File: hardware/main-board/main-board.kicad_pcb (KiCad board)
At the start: 2 copper layers, 48 x 48 mm, 44 parts, among them J1 USB-C Receptacle, J2 JST JWPF, J3 LCD_FFC_SOLDER, Q1 SS8050-G, Q2 SS8050-G, Q3 SS8050-G, SW1 FRONT_BUTTON, U1 SN65HVD230, U2 CPC1017N, U3 AP1509-33SG-13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

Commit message: layout almost done
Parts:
- moved D1 2.29 mm to (-14.1, 11.4)
- moved C3 1.91 mm to (12.8, 1.02)
- moved R11 0.51 mm to (-15.6, -2.41)
- moved R9 0.44 mm to (-15.7, 0.64)
- moved U4 0.38 mm to (-19.7, -0.60)
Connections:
- D1 pad 1: /USB_D+ -> /USB_D-
- D1 pad 3: /USB_D- -> /USB_D+
- R4 pad 2: (no net) -> /ESP32/CANBUS_TERM_EN
- U5 pad 24: (no net) -> /ESP32/CANBUS_TERM_EN
- U5 pad 39: (no net) -> GND
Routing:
- net +3V3: track 0.00 -> 62.4 mm, vias 0 -> 3
- net /USB_VBUS: track 0.00 -> 60.2 mm, vias 0 -> 4
- net /ESP32/EN: track 0.00 -> 55.0 mm, vias 0 -> 2
- net /ESP32/FRONT_BUTTON: track 0.00 -> 39.4 mm, vias 0 -> 1
- net /ESP32/PROG_TXD: track 0.00 -> 32.2 mm, vias 0 -> 2
- net /ESP32/PROG_RX: track 0.00 -> 32.2 mm, vias 0 -> 2
- net /USB_D+: track 0.00 -> 29.5 mm, vias 0 -> 2
- net /USB_D-: track 0.00 -> 27.0 mm, vias 0 -> 3
- net /ESP32/IO0: track 0.00 -> 24.3 mm, vias 0 -> 2
- net /LCD/BACKLIGHT: track 0.00 -> 22.6 mm, vias 0 -> 2
- net /ESP32/LCD_SDO: track 0.00 -> 22.5 mm, vias 0 -> 1
- net /ESP32/CANBUS_TX: track 0.00 -> 22.3 mm, vias 0 -> 2
- net /ESP32/CANBUS_RX: track 0.00 -> 21.1 mm, vias 0 -> 2
- net GND: track 0.00 -> 19.5 mm, vias 0 -> 10
- net /CANH: track 0.00 -> 18.7 mm
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- added copper zone on B.Cu, net GND
- added copper zone on F.Cu, net GND

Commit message: added all 3d
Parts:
- J1: footprint Connector_USB:USB_C_Receptacle_JAE_DX07S024WJ3R400 -> main-board-custom-footprints:USB_C_Receptacle_JAE_DX07S024WJ3R400
- J2: footprint Connector_JST:JST_JWPF_B04B-JWPF-SK-R_1x04_P2.00mm_Vertical -> main-board-custom-footprints:JST_JWPF_B04B-JWPF-SK-R_1x04_P2.00mm_Vertical
- L1: footprint Inductor_SMD:L_Taiyo-Yuden_NR-60xx -> main-board-custom-footprints:L_Taiyo-Yuden_NR-60xx
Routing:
- net +3V3: track 62.4 -> 117.3 mm, vias 3 -> 10
- net /ESP32/~RTS: track 3.19 -> 57.5 mm, vias 1 -> 4
- net /ESP32/~DTR: track 3.95 -> 36.8 mm
- net /USB_VBUS: track 60.2 -> 84.0 mm, vias 4 -> 5
- net GND: track 19.5 -> 24.2 mm, vias 10 -> 28
- net /ESP32/IO0: track 24.3 -> 24.8 mm
- net /ESP32/EN: track 55.0 -> 55.3 mm, vias 2 -> 4

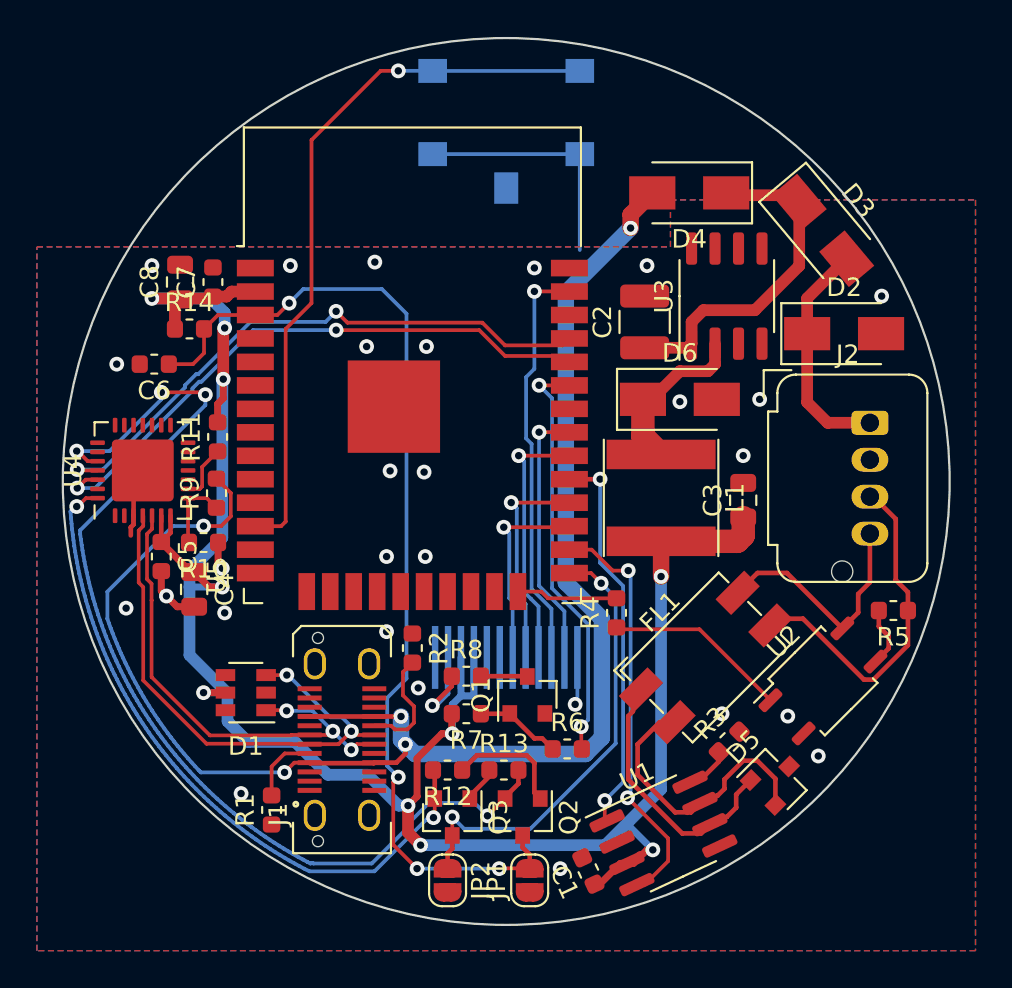
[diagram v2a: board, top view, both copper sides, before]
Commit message: SO-8 3d added, layout done
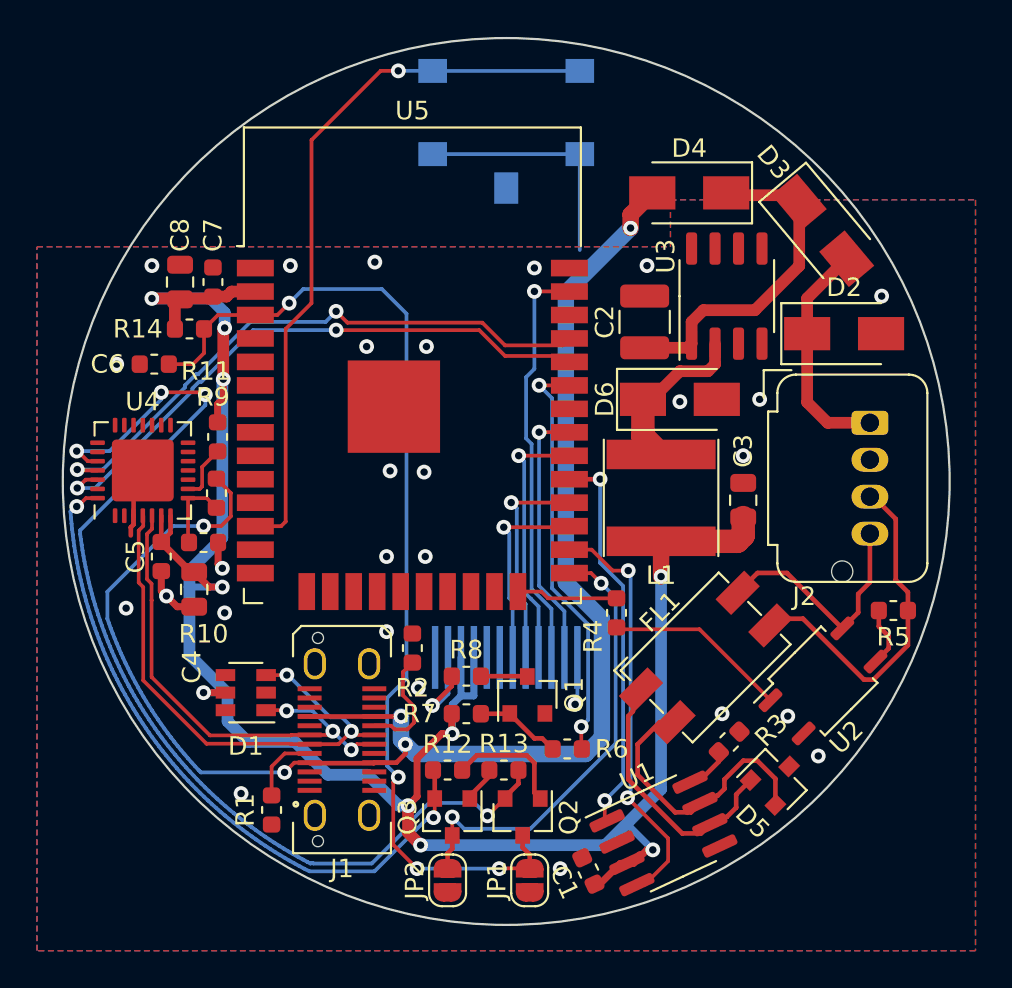
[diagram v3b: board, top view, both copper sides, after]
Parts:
- U3: footprint Package_SO:SO-8_3.9x4.9mm_P1.27mm -> main-board-custom-footprints:SO-8_3.9x4.9mm_P1.27mm
